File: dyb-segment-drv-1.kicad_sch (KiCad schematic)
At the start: 3 parts, among them U2 SN74AUP2G08, U3 74AUC2G32, U4 Inverter_Schmitt_Dual

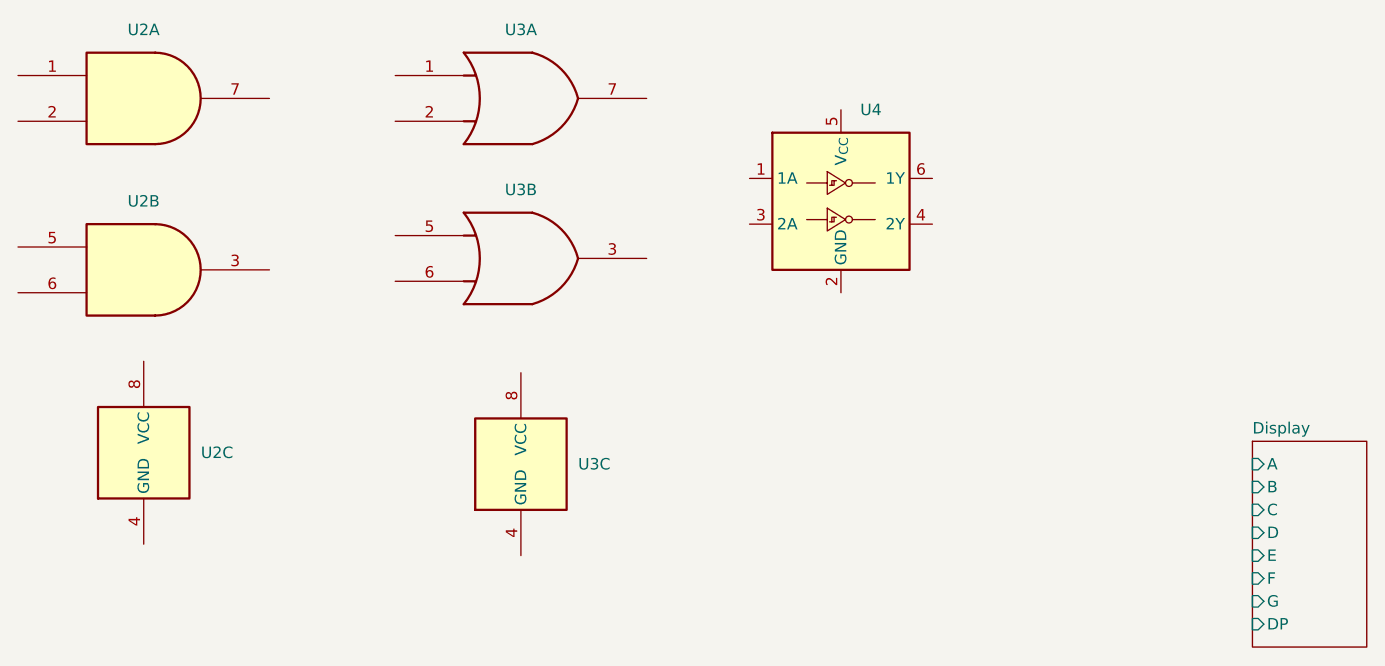
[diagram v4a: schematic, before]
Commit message: schem: add ab segment drivers
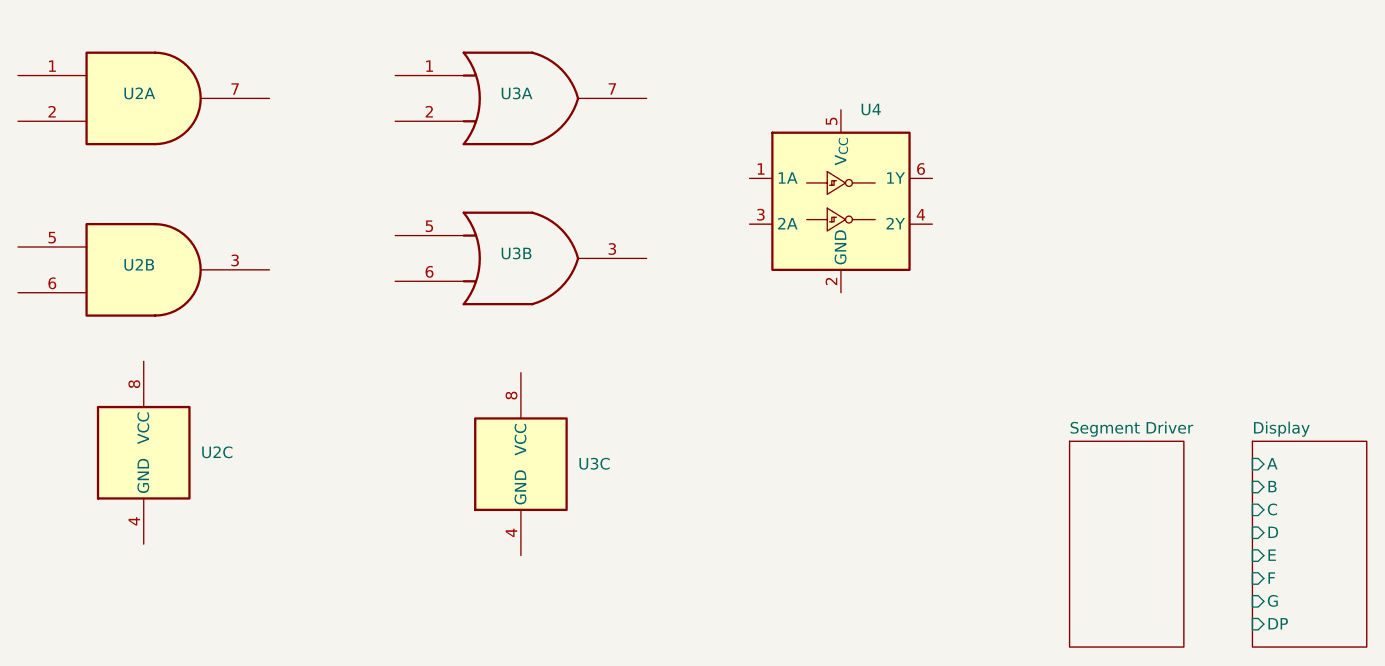
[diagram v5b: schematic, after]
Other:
- added sheet Segment Driver (driver.kicad_sch)
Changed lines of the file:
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@@
 		(in_pos_files yes)
 		(dnp no)
-		(fields_autoplaced yes)
 		(property "Reference" "U3"
-			(at 146.05 43.18 0)
+			(at 145.5531 50.292 0)
 			(show_name no)
 			(do_not_autoplace no)
@@
 		(in_pos_files yes)
 		(dnp no)
-		(fields_autoplaced yes)
 		(property "Reference" "U2"
-			(at 104.1289 25.4 0)
+			(at 103.632 32.512 0)
 			(show_name no)
 			(do_not_autoplace no)
@@
 		(in_pos_files yes)
 		(dnp no)
-		(fields_autoplaced yes)
 		(property "Reference" "U2"
-			(at 104.1289 44.45 0)
+			(at 103.632 51.562 0)
 			(show_name no)
 			(do_not_autoplace no)
@@
 		(in_pos_files yes)
 		(dnp no)
-		(fields_autoplaced yes)
 		(property "Reference" "U3"
-			(at 146.05 25.4 0)
+			(at 145.5531 32.512 0)
 			(show_name no)
 			(do_not_autoplace no)
@@
 				)
 			)
+		)
+	)
+	(sheet
+		(at 207.01 71.12)
+		(size 12.7 22.86)
+		(exclude_from_sim no)
+		(in_bom yes)
+		(on_board yes)
+		(dnp no)
+		(fields_autoplaced yes)
+		(stroke
+			(width 0.1524)
+			(type solid)
+		)
+		(fill
+			(color 0 0 0 0)
+		)
+		(property "Sheetname" "Segment Driver"
+			(at 207.01 70.4084 0)
+			(show_name no)
+			(do_not_autoplace no)
+			(effects
+				(font
+					(size 1.27 1.27)
+				)
+				(justify left bottom)
+			)
+		)
+		(property "Sheetfile" "driver.kicad_sch"
+			(at 207.01 94.5646 0)
+			(hide yes)
+			(show_name no)
+			(do_not_autoplace no)
+			(effects
+				(font
+					(size 1.27 1.27)
+				)
+				(justify left top)
+			)
+		)
+		(instances
+			(project "dyb-segment-drv-1"
+				(path "/0d1f997b-7d97-47c3-85c1-1ce9346504d0"
+					(page "3")
+				)
+			)

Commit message: schem: add d segment
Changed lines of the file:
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@@
 		(in_pos_files yes)
 		(dnp no)
-		(fields_autoplaced yes)
 		(property "Reference" "U2"
-			(at 110.49 72.3899 0)
+			(at 105.664 79.248 0)
 			(show_name no)
 			(do_not_autoplace no)
@@
 		(in_pos_files yes)
 		(dnp no)
-		(fields_autoplaced yes)
 		(property "Reference" "U3"
-			(at 152.4 73.6599 0)
+			(at 147.574 80.518 0)
 			(show_name no)
 			(do_not_autoplace no)

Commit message: schem: add second number
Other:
- added sheet Display1 (display.kicad_sch)
- added sheet Segment Driver1 (driver.kicad_sch)
- sheet Segment Driver ports: added A, B, C, D, D0, D1, D2, D3, DP, E, F, G; removed none

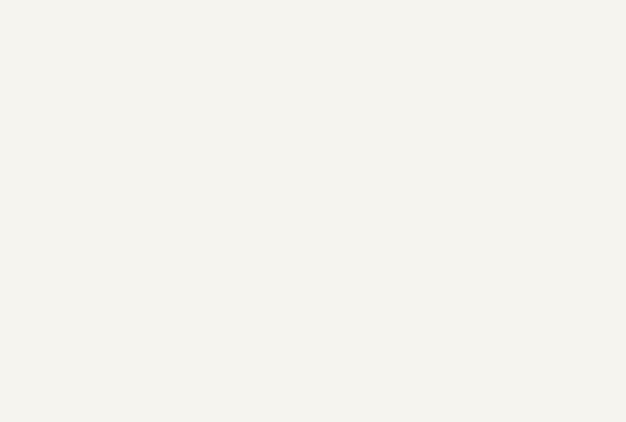
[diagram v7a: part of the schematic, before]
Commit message: schem: add AP2112K 1V8 LDO
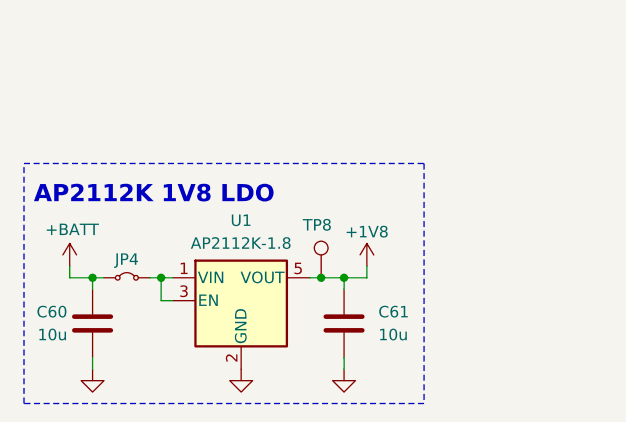
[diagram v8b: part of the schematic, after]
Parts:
- added C60, C61: 10u, Capacitor_SMD:C_0805_2012Metric, symbol Device:C
- added JP4: Jumper_2_Small_Bridged, Connector_PinHeader_2.54mm:PinHeader_1x02_P2.54mm_Vertical, symbol Jumper:Jumper_2_Small_Bridged
- added TP8: TestPoint, TestPoint:TestPoint_Pad_D2.0mm, symbol Connector:TestPoint
- added U1: AP2112K-1.8, Package_TO_SOT_SMD:SOT-23-5, symbol Regulator_Linear:AP2112K-1.8
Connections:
- new net: JP4.2 (B), U1.1 (VIN), U1.3 (EN)
- new net +1V8: C61.1, TP8.1, U1.5 (VOUT)
- new net +BATT: C60.1, JP4.1 (A)
- new net GND: C60.2, C61.2, U1.2 (GND)
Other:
- note added: "AP2112K 1V8 LDO"
